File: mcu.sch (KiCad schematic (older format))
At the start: 9 parts, among them P3 SWD, U3 LCD-2x16, U4 STM32F401xB/C-LQFP, U5 Thumb-Joystick

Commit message: Joystick is now 5-pin header and associated
Now we are ready to lay out the board!
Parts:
- removed U5: Thumb-Joystick, symbol Thumb-Joystick
- added P7: Thumb-Joystick, Pin_Headers:Pin_Header_Straight_1x05, symbol CONN_01X05
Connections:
- wire segments 41 -> 35
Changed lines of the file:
@@
-$EndComp
-$Comp
-L Thumb-Joystick U5
-U 1 1 54725DA4
-P 7950 3900
-F 0 "U5" H 7100 4125 60  0000 C CNN
-F 1 "Thumb-Joystick" H 7400 4050 60  0000 C CNN
-F 2 "" H 7950 2950 60  0001 C CNN
-F 3 "" H 7950 2950 60  0000 C CNN
-	1    7950 3900
-	-1   0    0    -1
 $EndComp
 $Comp
@@
 Wire Wire Line
 	4200 3900 4200 4100
-Wire Wire Line
-	6450 4000 7950 4000
-Wire Wire Line
-	6450 4100 7800 4100
-Wire Wire Line
-	7800 4100 7800 4300
-Wire Wire Line
-	7800 4300 7950 4300
-Wire Wire Line
-	7950 4500 7750 4500
-Wire Wire Line
-	7750 4500 7750 4200
-Wire Wire Line
-	7750 4200 6450 4200
-$Comp
-L GND #PWR081
-U 1 1 54725FF5
-P 7950 4650
-F 0 "#PWR081" H 7950 4650 30  0001 C CNN
-F 1 "GND" H 7950 4580 30  0001 C CNN
-F 2 "" H 7950 4650 60  0000 C CNN
-F 3 "" H 7950 4650 60  0000 C CNN
-	1    7950 4650
-	1    0    0    -1
-$EndComp
-$Comp
-L GND #PWR082
-U 1 1 54726000
-P 7900 4400
-F 0 "#PWR082" H 7900 4400 30  0001 C CNN
-F 1 "GND" H 7900 4330 30  0001 C CNN
-F 2 "" H 7900 4400 60  0000 C CNN
-F 3 "" H 7900 4400 60  0000 C CNN
-	1    7900 4400
-	0    1    1    0
-$EndComp
-$Comp
-L GND #PWR083
-U 1 1 5472600B
-P 7900 4100
-F 0 "#PWR083" H 7900 4100 30  0001 C CNN
-F 1 "GND" H 7900 4030 30  0001 C CNN
-F 2 "" H 7900 4100 60  0000 C CNN
-F 3 "" H 7900 4100 60  0000 C CNN
-	1    7900 4100
-	0    1    1    0
-$EndComp
-Wire Wire Line
-	7950 4100 7900 4100
-Wire Wire Line
-	7950 4400 7900 4400
-Wire Wire Line
-	7950 4600 7950 4650
-$Comp
-L +3.3V #PWR084
-U 1 1 5472608E
-P 7950 3900
-F 0 "#PWR084" H 7950 3860 30  0001 C CNN
-F 1 "+3.3V" H 7950 4010 30  0000 C CNN
-F 2 "" H 7950 3900 60  0000 C CNN
-F 3 "" H 7950 3900 60  0000 C CNN
-	1    7950 3900
-	1    0    0    -1
-$EndComp
-$Comp
-L +3.3V #PWR085
-U 1 1 54726099
-P 7950 4200
-F 0 "#PWR085" H 7950 4160 30  0001 C CNN
-F 1 "+3.3V" H 7950 4310 30  0000 C CNN
-F 2 "" H 7950 4200 60  0000 C CNN
-F 3 "" H 7950 4200 60  0000 C CNN
-	1    7950 4200
-	0    -1   -1   0
-$EndComp
 Text HLabel 6500 2400 2    60   Output ~ 0
 mcu_band1
@@
 Wire Wire Line
 	6500 3300 6450 3300
+$Comp
+L CONN_01X05 P7
+U 1 1 54833D53
+P 7600 4100
+F 0 "P7" H 7600 4400 50  0000 C CNN
+F 1 "Thumb-Joystick" V 7700 4100 50  0000 C CNN
+F 2 "Pin_Headers:Pin_Header_Straight_1x05" H 7600 4100 60  0001 C CNN
+F 3 "" H 7600 4100 60  0000 C CNN
+	1    7600 4100
+	1    0    0    -1
+$EndComp
+$Comp
+L +3.3V #PWR081
+U 1 1 54833E0A
+P 7400 3900
+F 0 "#PWR081" H 7400 3860 30  0001 C CNN
+F 1 "+3.3V" H 7400 4010 30  0000 C CNN
+F 2 "" H 7400 3900 60  0000 C CNN
+F 3 "" H 7400 3900 60  0000 C CNN
+	1    7400 3900
+	1    0    0    -1
+$EndComp
+$Comp
+L GND #PWR082
+U 1 1 54833E38
+P 7300 4300
+F 0 "#PWR082" H 7300 4300 30  0001 C CNN
+F 1 "GND" H 7300 4230 30  0001 C CNN
+F 2 "" H 7300 4300 60  0000 C CNN
+F 3 "" H 7300 4300 60  0000 C CNN
+	1    7300 4300
+	0    1    1    0
+$EndComp
+Wire Wire Line
+	7400 4300 7300 4300
+Wire Wire Line
+	6450 4000 7400 4000
+Wire Wire Line
+	7400 4100 6450 4100
+Wire Wire Line
+	6450 4200 7400 4200
 $EndSCHEMATC

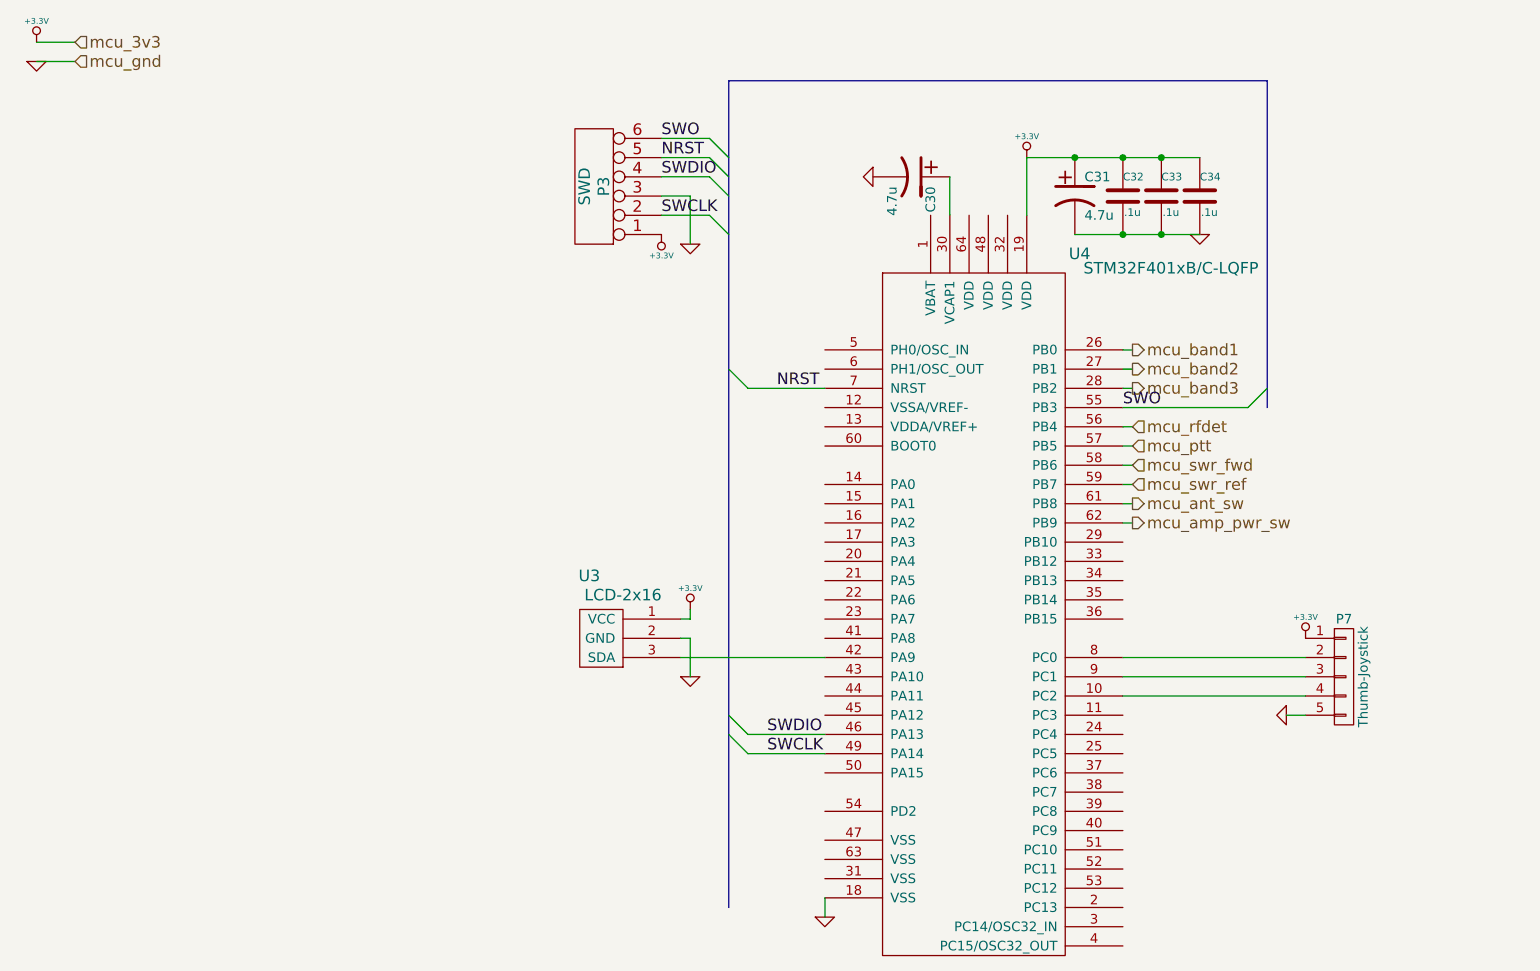
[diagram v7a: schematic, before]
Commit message: Separate analog/digital gnd. Add some filtering caps and reset button.
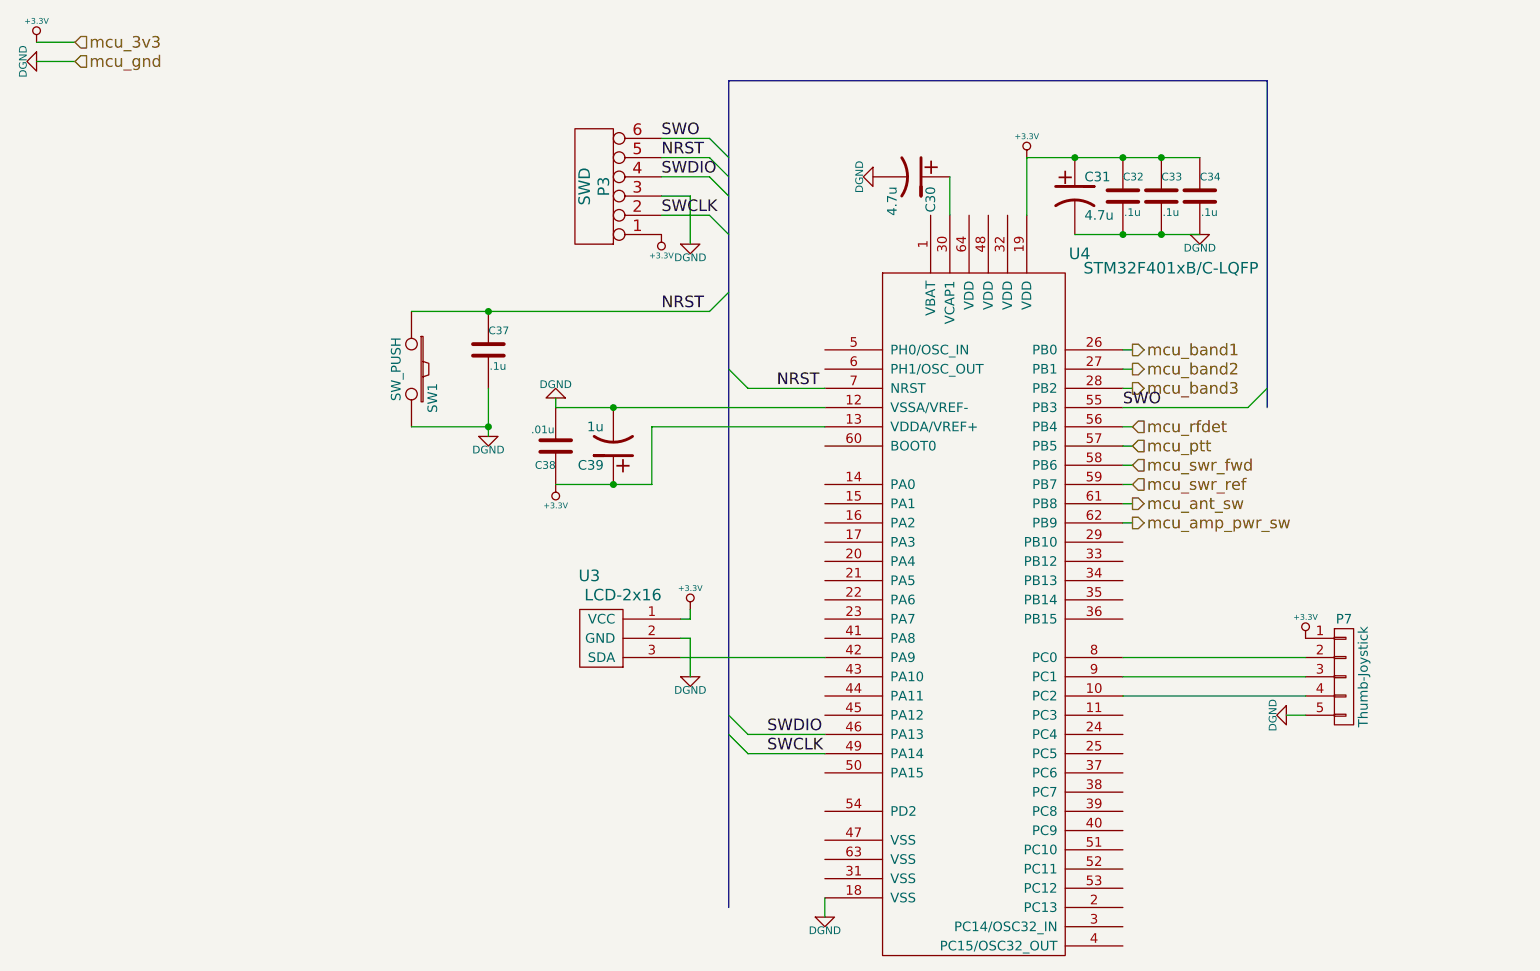
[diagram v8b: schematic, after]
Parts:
- added C37: .1u, Capacitors_SMD:C_0805_HandSoldering, symbol C
- added C38: .01u, Capacitors_SMD:C_0805_HandSoldering, symbol C
- added C39: 1u, Capacitors_ThroughHole:Capacitor5x11RM2.5, symbol CP1
- added SW1: SW_PUSH, Pin_Headers:Pin_Header_Straight_1x02, symbol SW_PUSH
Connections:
- net GND is gone; now on net DGND: C30.2, C31.2, C32.2, C33.2, C34.2, P3.3, P7.5 (P5), U3.2 (GND), U4.18 (VSS)
- net +3.3V: now also U4.13 (VDDA/VREF+), C38.1, C39.1
- net NRST: now also C37.1, SW1.1
- net DGND: now reaches U4.12 (VSSA/VREF-)
- net DGND: now also C37.2, C38.2, C39.2, SW1.2
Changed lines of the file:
@@
-$EndComp
-$Comp
-L GND #PWR071
-U 1 1 547253A0
-P 5150 1500
-F 0 "#PWR071" H 5150 1500 30  0001 C CNN
-F 1 "GND" H 5150 1430 30  0001 C CNN
-F 2 "" H 5150 1500 60  0000 C CNN
-F 3 "" H 5150 1500 60  0000 C CNN
-	1    5150 1500
-	0    1    1    0
 $EndComp
 $Comp
@@
 $EndComp
 $Comp
-L GND #PWR072
-U 1 1 54725403
-P 6850 1800
-F 0 "#PWR072" H 6850 1800 30  0001 C CNN
-F 1 "GND" H 6850 1730 30  0001 C CNN
-F 2 "" H 6850 1800 60  0000 C CNN
-F 3 "" H 6850 1800 60  0000 C CNN
-	1    6850 1800
-	1    0    0    -1
-$EndComp
-$Comp
-L GND #PWR073
-U 1 1 5472548C
-P 4900 5350
-F 0 "#PWR073" H 4900 5350 30  0001 C CNN
-F 1 "GND" H 4900 5280 30  0001 C CNN
-F 2 "" H 4900 5350 60  0000 C CNN
-F 3 "" H 4900 5350 60  0000 C CNN
-	1    4900 5350
-	1    0    0    -1
-$EndComp
-$Comp
-L GND #PWR074
-U 1 1 547254B6
-P 4200 1850
-F 0 "#PWR074" H 4200 1850 30  0001 C CNN
-F 1 "GND" H 4200 1780 30  0001 C CNN
-F 2 "" H 4200 1850 60  0000 C CNN
-F 3 "" H 4200 1850 60  0000 C CNN
-	1    4200 1850
-	1    0    0    -1
-$EndComp
-$Comp
-L +3.3V #PWR075
+L +3.3V #PWR074
 U 1 1 547254E1
 P 5950 1400
-F 0 "#PWR075" H 5950 1360 30  0001 C CNN
+F 0 "#PWR074" H 5950 1360 30  0001 C CNN
 F 1 "+3.3V" H 5950 1510 30  0000 C CNN
 F 2 "" H 5950 1400 60  0000 C CNN
@@
 $EndComp
 $Comp
-L +3.3V #PWR076
+L +3.3V #PWR075
 U 1 1 547254F3
 P 4050 1800
-F 0 "#PWR076" H 4050 1760 30  0001 C CNN
+F 0 "#PWR075" H 4050 1760 30  0001 C CNN
 F 1 "+3.3V" H 4050 1910 30  0000 C CNN
 F 2 "" H 4050 1800 60  0000 C CNN
@@
 $EndComp
 $Comp
-L +3.3V #PWR077
+L +3.3V #PWR076
 U 1 1 547256B9
 P 800 800
-F 0 "#PWR077" H 800 760 30  0001 C CNN
+F 0 "#PWR076" H 800 760 30  0001 C CNN
 F 1 "+3.3V" H 800 910 30  0000 C CNN
 F 2 "" H 800 800 60  0000 C CNN
@@
 	1    0    0    -1
 $EndComp
-$Comp
-L GND #PWR078
-U 1 1 547256C4
-P 800 900
-F 0 "#PWR078" H 800 900 30  0001 C CNN
-F 1 "GND" H 800 830 30  0001 C CNN
-F 2 "" H 800 900 60  0000 C CNN
-F 3 "" H 800 900 60  0000 C CNN
-	1    800  900
-	1    0    0    -1
-$EndComp
 Text HLabel 1000 800  2    60   Input ~ 0
 mcu_3v3
@@
 mcu_gnd
 $Comp
-L +3.3V #PWR079
+L +3.3V #PWR077
 U 1 1 54725A58
 P 4200 3750
-F 0 "#PWR079" H 4200 3710 30  0001 C CNN
+F 0 "#PWR077" H 4200 3710 30  0001 C CNN
 F 1 "+3.3V" H 4200 3860 30  0000 C CNN
 F 2 "" H 4200 3750 60  0000 C CNN
 F 3 "" H 4200 3750 60  0000 C CNN
 	1    4200 3750
-	1    0    0    -1
-$EndComp
-$Comp
-L GND #PWR080
-U 1 1 54725A7F
-P 4200 4100
-F 0 "#PWR080" H 4200 4100 30  0001 C CNN
-F 1 "GND" H 4200 4030 30  0001 C CNN
-F 2 "" H 4200 4100 60  0000 C CNN
-F 3 "" H 4200 4100 60  0000 C CNN
-	1    4200 4100
 	1    0    0    -1
 $EndComp
@@
 $EndComp
 $Comp
-L +3.3V #PWR081
+L +3.3V #PWR078
 U 1 1 54833E0A
 P 7400 3900
-F 0 "#PWR081" H 7400 3860 30  0001 C CNN
+F 0 "#PWR078" H 7400 3860 30  0001 C CNN
 F 1 "+3.3V" H 7400 4010 30  0000 C CNN
 F 2 "" H 7400 3900 60  0000 C CNN
@@
 	1    0    0    -1
 $EndComp
-$Comp
-L GND #PWR082
-U 1 1 54833E38
+Wire Wire Line
+	7400 4300 7300 4300
+Wire Wire Line
+	6450 4000 7400 4000
+Wire Wire Line
+	7400 4100 6450 4100
+Wire Wire Line
+	6450 4200 7400 4200
+$Comp
+L CP1 C39
+U 1 1 548452A0
+P 3800 2900
+F 0 "C39" H 3850 3000 50  0000 L CNN
+F 1 "1u" H 3850 2800 50  0000 L CNN
+F 2 "Capacitors_ThroughHole:Capacitor5x11RM2.5" H 3800 2900 60  0001 C CNN
+F 3 "" H 3800 2900 60  0000 C CNN
+	1    3800 2900
+	-1   0    0    1
+$EndComp
+$Comp
+L C C38
+U 1 1 54845340
+P 3500 2900
+F 0 "C38" H 3500 3000 40  0000 L CNN
+F 1 ".01u" H 3506 2815 40  0000 L CNN
+F 2 "Capacitors_SMD:C_0805_HandSoldering" H 3538 2750 30  0001 C CNN
+F 3 "" H 3500 2900 60  0000 C CNN
+	1    3500 2900
+	-1   0    0    1
+$EndComp
+Wire Wire Line
+	4900 2800 4000 2800
+Wire Wire Line
+	4000 2800 4000 3100
+Connection ~ 3800 3100
+Wire Wire Line
+	3500 2700 4900 2700
+Connection ~ 3800 2700
+$Comp
+L +3.3V #PWR079
+U 1 1 54845508
+P 3500 3100
+F 0 "#PWR079" H 3500 3060 30  0001 C CNN
+F 1 "+3.3V" H 3500 3210 30  0000 C CNN
+F 2 "" H 3500 3100 60  0000 C CNN
+F 3 "" H 3500 3100 60  0000 C CNN
+	1    3500 3100
+	-1   0    0    1
+$EndComp
+Wire Wire Line
+	3500 2700 3500 2650
+Wire Wire Line
+	4000 3100 3500 3100
+Entry Wire Line
+	4300 2200 4400 2100
+$Comp
+L C C37
+U 1 1 54845A82
+P 3150 2400
+F 0 "C37" H 3150 2500 40  0000 L CNN
+F 1 ".1u" H 3156 2315 40  0000 L CNN
+F 2 "Capacitors_SMD:C_0805_HandSoldering" H 3188 2250 30  0001 C CNN
+F 3 "" H 3150 2400 60  0000 C CNN
+	1    3150 2400
+	1    0    0    -1
+$EndComp
+Wire Wire Line
+	2750 2200 4300 2200
+Text Label 4050 2200 0    60   ~ 0
+NRST
+$Comp
+L DGND #PWR080
+U 1 1 54845B65
+P 3150 2850
+F 0 "#PWR080" H 3150 2850 40  0001 C CNN
+F 1 "DGND" H 3150 2780 40  0000 C CNN
+F 2 "" H 3150 2850 60  0000 C CNN
+F 3 "" H 3150 2850 60  0000 C CNN
+	1    3150 2850
+	1    0    0    -1
+$EndComp
+Wire Wire Line
+	3150 2600 3150 2850
+$Comp
+L SW_PUSH SW1
+U 1 1 54845BBA
+P 2750 2500
+F 0 "SW1" H 2900 2610 50  0000 C CNN
+F 1 "SW_PUSH" H 2750 2420 50  0000 C CNN
+F 2 "Pin_Headers:Pin_Header_Straight_1x02" H 2750 2500 60  0001 C CNN
+F 3 "" H 2750 2500 60  0000 C CNN
+	1    2750 2500
+	0    1    1    0
+$EndComp
+Connection ~ 3150 2200
+Wire Wire Line
+	2750 2800 3150 2800
+Connection ~ 3150 2800
+$Comp
+L DGND #PWR081
+U 1 1 54845CF0
+P 3500 2650
+F 0 "#PWR081" H 3500 2650 40  0001 C CNN
+F 1 "DGND" H 3500 2580 40  0000 C CNN
+F 2 "" H 3500 2650 60  0000 C CNN
+F 3 "" H 3500 2650 60  0000 C CNN
+	1    3500 2650
+	-1   0    0    1
+$EndComp
+$Comp
+L DGND #PWR082
+U 1 1 54845D08
+P 4200 4100
+F 0 "#PWR082" H 4200 4100 40  0001 C CNN
+F 1 "DGND" H 4200 4030 40  0000 C CNN
+F 2 "" H 4200 4100 60  0000 C CNN
+F 3 "" H 4200 4100 60  0000 C CNN
+	1    4200 4100
+	1    0    0    -1
+$EndComp
+$Comp
+L DGND #PWR083
+U 1 1 54845D53
+P 4200 1850
+F 0 "#PWR083" H 4200 1850 40  0001 C CNN
+F 1 "DGND" H 4200 1780 40  0000 C CNN
+F 2 "" H 4200 1850 60  0000 C CNN
+F 3 "" H 4200 1850 60  0000 C CNN
+	1    4200 1850
+	1    0    0    -1
+$EndComp
+$Comp
+L DGND #PWR084
+U 1 1 54845DAD
+P 4900 5350
+F 0 "#PWR084" H 4900 5350 40  0001 C CNN
+F 1 "DGND" H 4900 5280 40  0000 C CNN
+F 2 "" H 4900 5350 60  0000 C CNN
+F 3 "" H 4900 5350 60  0000 C CNN
+	1    4900 5350
+	1    0    0    -1
+$EndComp
+$Comp
+L DGND #PWR085
+U 1 1 54845DDF
+P 5150 1500
+F 0 "#PWR085" H 5150 1500 40  0001 C CNN
+F 1 "DGND" H 5150 1430 40  0000 C CNN
+F 2 "" H 5150 1500 60  0000 C CNN
+F 3 "" H 5150 1500 60  0000 C CNN
+	1    5150 1500
+	0    1    1    0
+$EndComp
+$Comp
+L DGND #PWR086
+U 1 1 54845E05
 P 7300 4300
-F 0 "#PWR082" H 7300 4300 30  0001 C CNN
-F 1 "GND" H 7300 4230 30  0001 C CNN
+F 0 "#PWR086" H 7300 4300 40  0001 C CNN
+F 1 "DGND" H 7300 4230 40  0000 C CNN
 F 2 "" H 7300 4300 60  0000 C CNN
 F 3 "" H 7300 4300 60  0000 C CNN
@@
 	0    1    1    0
 $EndComp
-Wire Wire Line
-	7400 4300 7300 4300
-Wire Wire Line
-	6450 4000 7400 4000
-Wire Wire Line
-	7400 4100 6450 4100
-Wire Wire Line
-	6450 4200 7400 4200
+$Comp
+L DGND #PWR087
+U 1 1 54845E90
+P 6850 1800
+F 0 "#PWR087" H 6850 1800 40  0001 C CNN
+F 1 "DGND" H 6850 1730 40  0000 C CNN
+F 2 "" H 6850 1800 60  0000 C CNN
+F 3 "" H 6850 1800 60  0000 C CNN
+	1    6850 1800
+	1    0    0    -1
+$EndComp
+$Comp
+L DGND #PWR088
+U 1 1 5484639A
+P 800 900
+F 0 "#PWR088" H 800 900 40  0001 C CNN
+F 1 "DGND" H 800 830 40  0000 C CNN
+F 2 "" H 800 900 60  0000 C CNN
+F 3 "" H 800 900 60  0000 C CNN
+	1    800  900
+	0    1    1    0
+$EndComp
 $EndSCHEMATC
